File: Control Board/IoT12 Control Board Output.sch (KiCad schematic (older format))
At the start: 24 parts, among them Q1 MMBT2222, Q2 MMBT2222, Q3 AOD403

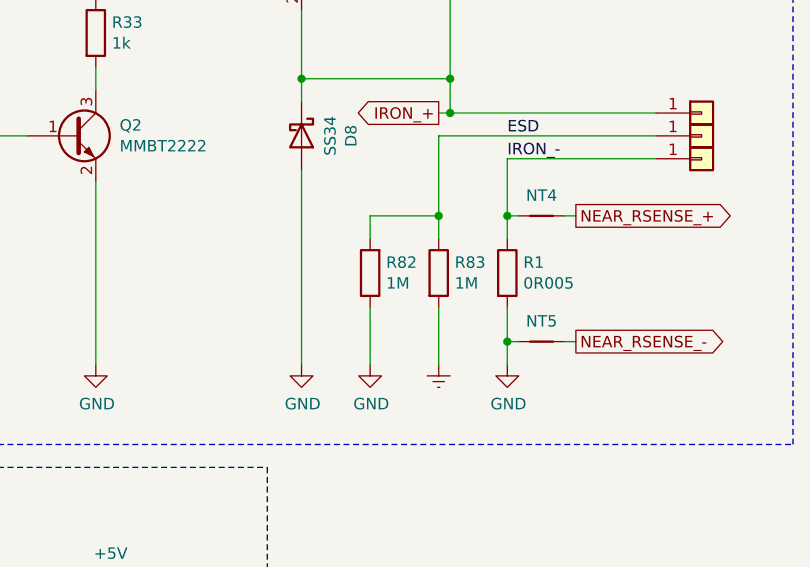
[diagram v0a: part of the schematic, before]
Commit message: Changed value R82.
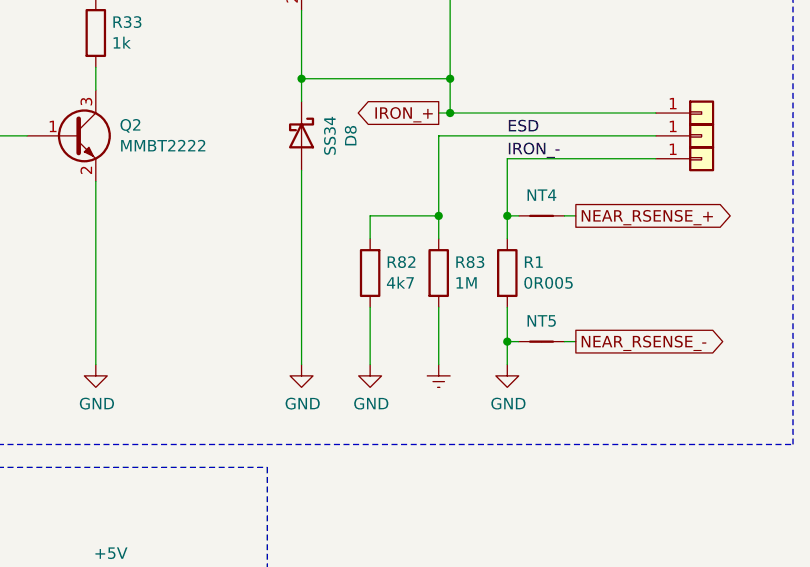
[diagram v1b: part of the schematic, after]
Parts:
- R82: value 1M -> 4k7
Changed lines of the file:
@@
 P 3900 3350
 F 0 "R82" H 3830 3304 50  0000 R CNN
-F 1 "1M" H 3830 3395 50  0000 R CNN
+F 1 "4k7" H 3830 3395 50  0000 R CNN
 F 2 "Resistor_SMD:R_0805_2012Metric_Pad1.20x1.40mm_HandSolder" V 3830 3350 50  0001 C CNN
 F 3 "~" H 3900 3350 50  0001 C CNN

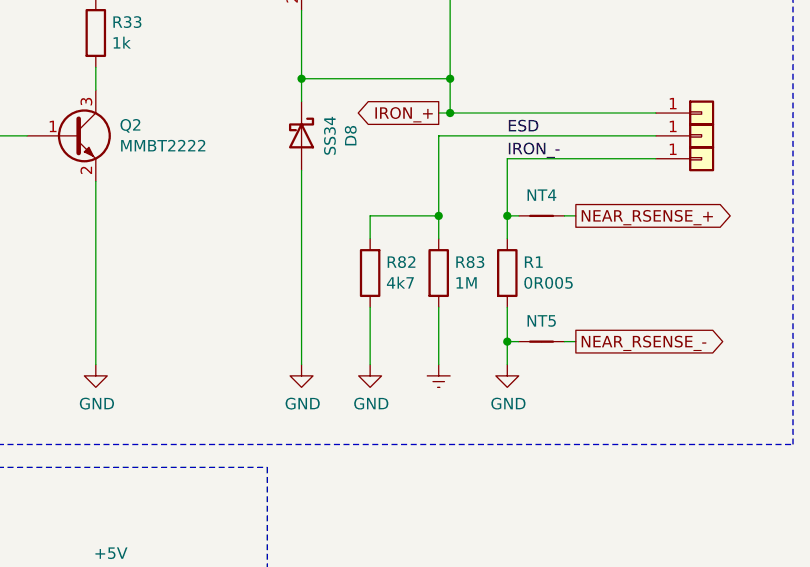
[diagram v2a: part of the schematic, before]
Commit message: Revert R82 back to 1M.
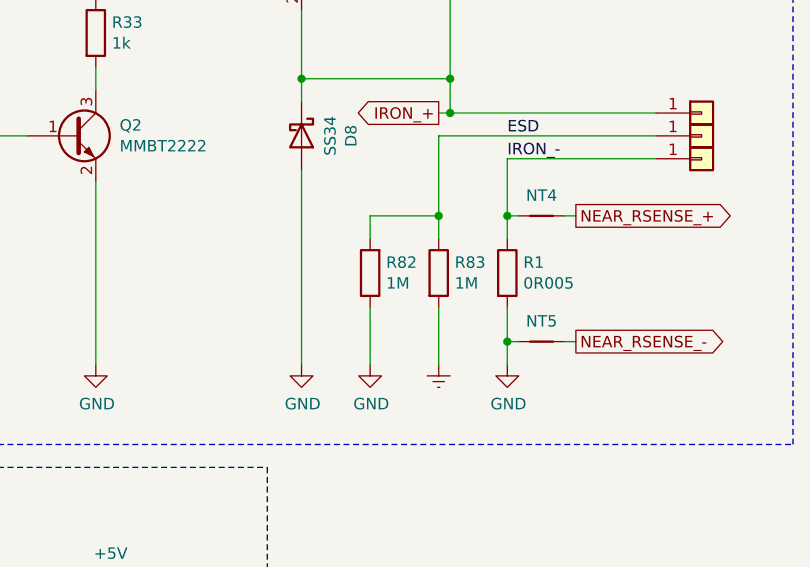
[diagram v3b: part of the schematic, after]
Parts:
- R82: value 4k7 -> 1M
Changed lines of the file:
@@
 Sheet 5 5
 Title "IoT12-hardware output"
-Date "2021-03-27"
+Date "2021-03-28"
 Rev "V2.1"
 Comp ""
@@
 P 3900 3350
 F 0 "R82" H 3830 3304 50  0000 R CNN
-F 1 "4k7" H 3830 3395 50  0000 R CNN
+F 1 "1M" H 3830 3395 50  0000 R CNN
 F 2 "Resistor_SMD:R_0805_2012Metric_Pad1.20x1.40mm_HandSolder" V 3830 3350 50  0001 C CNN
 F 3 "~" H 3900 3350 50  0001 C CNN
